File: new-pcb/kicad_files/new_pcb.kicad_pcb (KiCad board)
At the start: 2 copper layers, 98 x 81.6 mm, 39 parts, among them K0 KEYSW, K1 KEYSW, K10 KEYSW, K11 KEYSW, K12 KEYSW, K13 KEYSW, K2 KEYSW, K20 KEYSW, K21 KEYSW, K22 KEYSW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

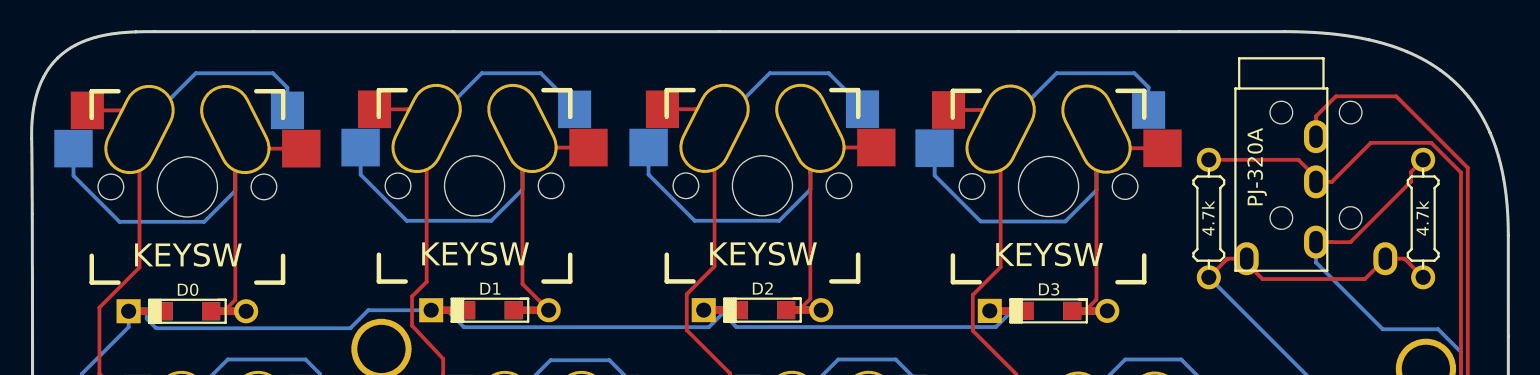
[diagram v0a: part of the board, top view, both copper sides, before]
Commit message: Add filled zones.
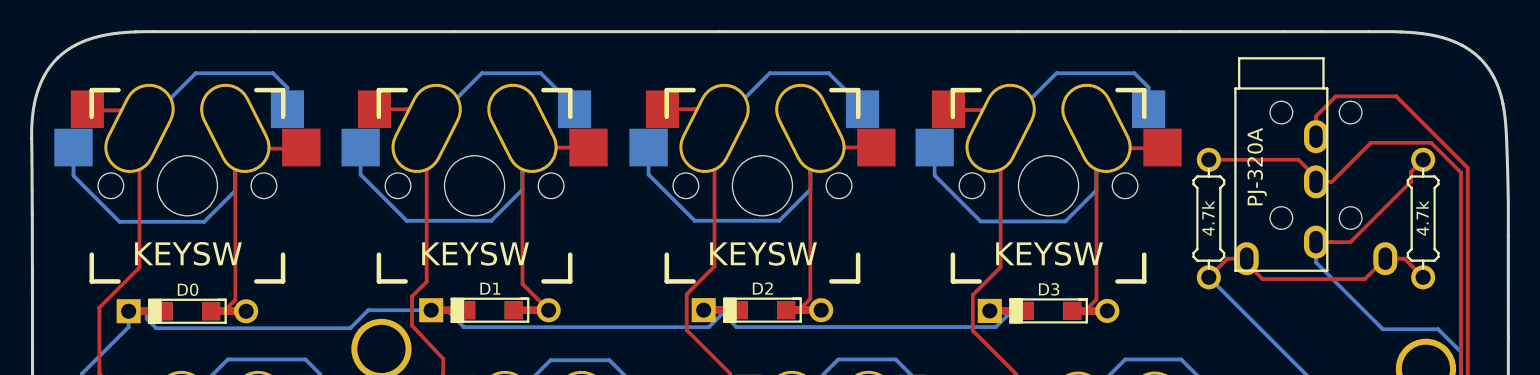
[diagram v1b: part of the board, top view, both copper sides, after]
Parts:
- moved K0 0.08 mm to (92.1, 60.9)
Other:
- outline, holes or cut-outs redrawn
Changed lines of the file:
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@@
-(kicad_pcb (version 20171130) (host pcbnew "(6.0.0-rc1-dev-1469-g932b9a334)")
+(kicad_pcb (version 20171130) (host pcbnew "(5.1.2-1)-1")
   (general
     (thickness 1.6)
-    (drawings 127)
+    (drawings 130)
     (tracks 420)
     (zones 0)
@@
   )
   (module new_pcb_footprints:Mx_hotswappable_oval (layer F.Cu)
-    (at 111.18 60.935)
+    (at 111.18 60.93)
     (descr "MX-style keyswitch with Kailh socket mount")
     (tags MX,cherry,gateron,kailh,pg1511,socket)
@@
   )
   (module new_pcb_footprints:Mx_hotswappable_oval (layer F.Cu)
-    (at 149.28 60.98)
+    (at 149.28 60.93)
     (descr "MX-style keyswitch with Kailh socket mount")
     (tags MX,cherry,gateron,kailh,pg1511,socket)
@@
   )
   (module new_pcb_footprints:Mx_hotswappable_oval (layer F.Cu)
-    (at 92.12 61.005)
+    (at 92.12 60.93)
     (descr "MX-style keyswitch with Kailh socket mount")
     (tags MX,cherry,gateron,kailh,pg1511,socket)
@@
       (xy -9.943822 1.795852)) (layer B.SilkS) (width 0.01))
   )
+  (gr_curve (pts (xy 179.68 57.76) (xy 179.642139 56.916852) (xy 179.574452 56.146128) (xy 179.437228 55.471054)) (layer Edge.Cuts) (width 0.2))
+  (gr_curve (pts (xy 179.437228 55.471054) (xy 179.300004 54.79598) (xy 179.093242 54.216556) (xy 178.832014 53.719231)) (layer Edge.Cuts) (width 0.2))
+  (gr_curve (pts (xy 178.832014 53.719231) (xy 178.570786 53.221906) (xy 178.255091 52.80668) (xy 177.9 52.46)) (layer Edge.Cuts) (width 0.2))
+  (gr_curve (pts (xy 177.9 52.46) (xy 177.54491 52.113321) (xy 177.150423 51.835189) (xy 176.731612 51.612052)) (layer Edge.Cuts) (width 0.2))
+  (gr_curve (pts (xy 176.731612 51.612052) (xy 176.312801 51.388916) (xy 175.869664 51.220774) (xy 175.417274 51.094077)) (layer Edge.Cuts) (width 0.2))
+  (gr_curve (pts (xy 175.417274 51.094077) (xy 174.964884 50.967379) (xy 174.50324 50.882126) (xy 174.047412 50.824764)) (layer Edge.Cuts) (width 0.2))
+  (gr_curve (pts (xy 174.047412 50.824764) (xy 173.591585 50.767402) (xy 173.141574 50.737933) (xy 172.712451 50.722803)) (layer Edge.Cuts) (width 0.2))
+  (gr_curve (pts (xy 167.42 50.7) (xy 166.87 50.7) (xy 165.71 50.7) (xy 164.916487 50.7)) (layer Edge.Cuts) (width 0.2))
   (gr_curve (pts (xy 161.095614 128.694384) (xy 160.159829 128.694384) (xy 159.401227 127.935779) (xy 159.401227 127)) (layer Eco1.User) (width 0.2))
   (gr_curve (pts (xy 159.401227 127) (xy 159.401227 126.064221) (xy 160.159829 125.305616) (xy 161.095614 125.305616)) (layer Eco1.User) (width 0.2))
@@
   (gr_curve (pts (xy 179.8 70.963392) (xy 179.8 73.928609) (xy 179.8 77.531869) (xy 179.8 81.539302)) (layer Edge.Cuts) (width 0.2))
   (gr_curve (pts (xy 179.795992 64.215737) (xy 179.794445 65.671001) (xy 179.796172 67.998175) (xy 179.800281 70.963392)) (layer Edge.Cuts) (width 0.2))
-  (gr_curve (pts (xy 179.482085 60.429541) (xy 179.688777 61.562322) (xy 179.797475 62.820181) (xy 179.795992 64.215737)) (layer Edge.Cuts) (width 0.2))
-  (gr_curve (pts (xy 178.580213 57.393816) (xy 178.970707 58.289058) (xy 179.275393 59.296761) (xy 179.482085 60.429541)) (layer Edge.Cuts) (width 0.2))
-  (gr_curve (pts (xy 177.163498 55.032848) (xy 177.713419 55.71579) (xy 178.18972 56.498573) (xy 178.580213 57.393816)) (layer Edge.Cuts) (width 0.2))
-  (gr_curve (pts (xy 175.305059 53.270926) (xy 175.990034 53.766805) (xy 176.613576 54.349906) (xy 177.163498 55.032848)) (layer Edge.Cuts) (width 0.2))
-  (gr_curve (pts (xy 173.078018 52.032338) (xy 173.873674 52.366391) (xy 174.620083 52.775048) (xy 175.305059 53.270926)) (layer Edge.Cuts) (width 0.2))
-  (gr_curve (pts (xy 170.555495 51.241371) (xy 171.437458 51.438836) (xy 172.282361 51.698285) (xy 173.078018 52.032338)) (layer Edge.Cuts) (width 0.2))
-  (gr_curve (pts (xy 167.810611 50.822314) (xy 168.754508 50.908427) (xy 169.673531 51.043907) (xy 170.555495 51.241371)) (layer Edge.Cuts) (width 0.2))
-  (gr_curve (pts (xy 164.916487 50.699453) (xy 165.897944 50.699453) (xy 166.866714 50.7362) (xy 167.810611 50.822314)) (layer Edge.Cuts) (width 0.2))
+  (gr_curve (pts (xy 179.68 57.76) (xy 179.83 61.69) (xy 179.797475 62.820181) (xy 179.795992 64.215737)) (layer Edge.Cuts) (width 0.2))
+  (gr_curve (pts (xy 170.53 50.7) (xy 171.437458 50.7) (xy 172.11 50.69) (xy 172.712451 50.722803)) (layer Edge.Cuts) (width 0.2))
+  (gr_curve (pts (xy 167.42 50.7) (xy 168.82 50.7) (xy 169.73 50.7) (xy 170.53 50.7)) (layer Edge.Cuts) (width 0.2))
   (gr_curve (pts (xy 157.98 50.7) (xy 161.501952 50.699453) (xy 163.935031 50.699453) (xy 164.916487 50.699453)) (layer Edge.Cuts) (width 0.2))
   (gr_curve (pts (xy 147.305545 50.699453) (xy 154.063878 50.699453) (xy 156.829614 50.699453) (xy 157.96 50.699453)) (layer Edge.Cuts) (width 0.2))

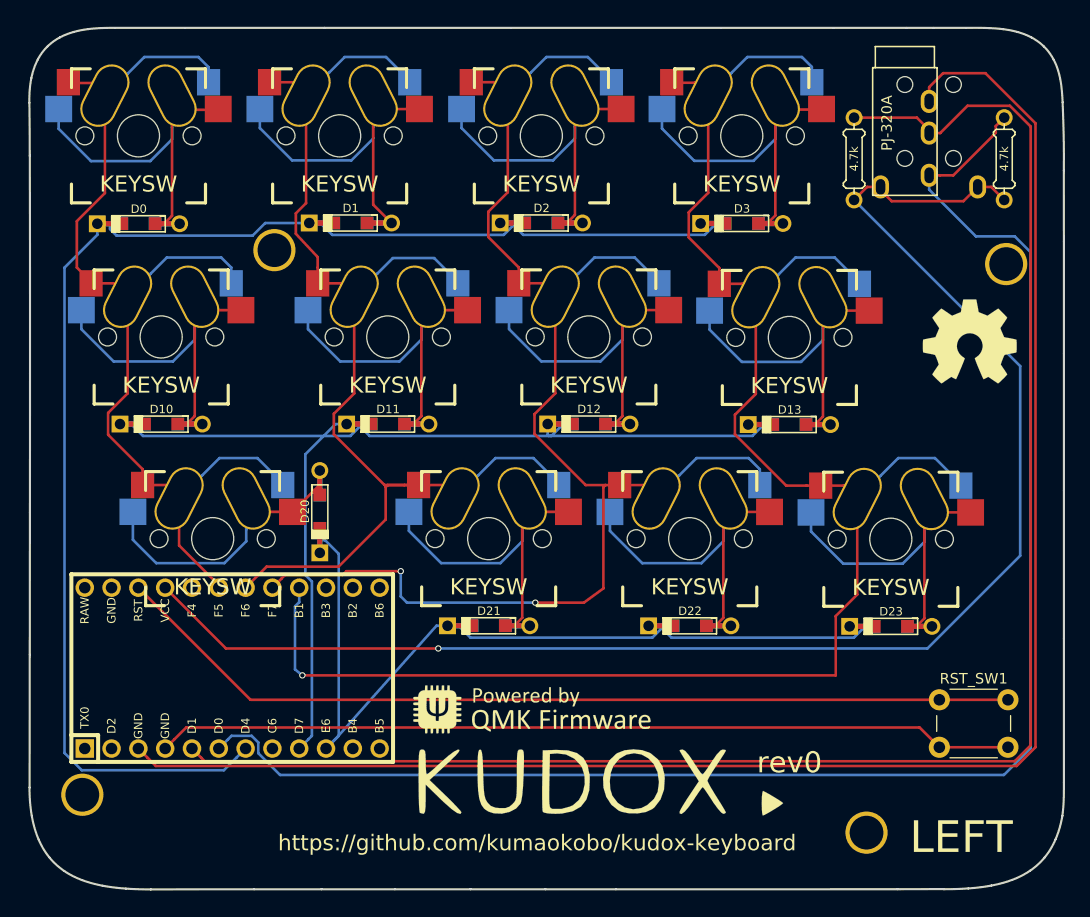
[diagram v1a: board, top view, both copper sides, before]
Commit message: Modified kudox-xs and new-pcb.
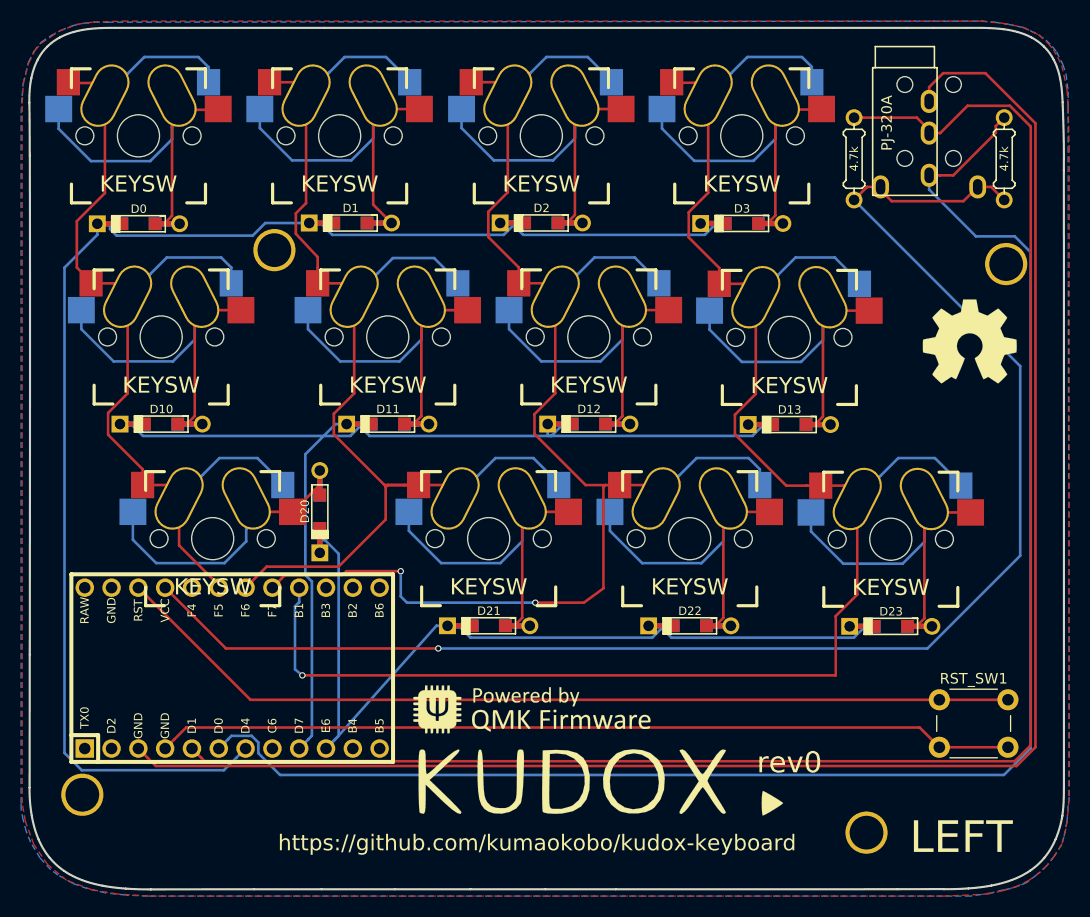
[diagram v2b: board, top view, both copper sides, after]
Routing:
- added copper zone on B.Cu, net (none)
- added copper zone on F.Cu, net (none)
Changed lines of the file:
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@@
-(kicad_pcb (version 20171130) (host pcbnew "(5.1.2-1)-1")
+(kicad_pcb (version 20171130) (host pcbnew "(6.0.0-rc1-dev-1469-g932b9a334)")
   (general
     (thickness 1.6)
@@
   (segment (start 102.73 114.36) (end 92.11 103.74) (width 0.25) (layer F.Cu) (net 30))
   (segment (start 168 114.36) (end 102.73 114.36) (width 0.25) (layer F.Cu) (net 30))
+  (zone (net 0) (net_name "") (layer F.Cu) (hatch edge 0.508)
+    (connect_pads (clearance 0.508))
+    (min_thickness 0.254)
+    (fill yes (arc_segments 16) (thermal_gap 0.508) (thermal_bridge_width 0.508))
+    (polygon
+      (pts
+        (xy 180.3 61.96) (xy 180.3 123.76) (xy 180.2 124.86) (xy 180 126.56) (xy 179.6 128.06)
+        (xy 178.9 129.16) (xy 178.2 130.06) (xy 177.6 130.66) (xy 176.5 131.46) (xy 175.3 132.06)
+        (xy 174 132.46) (xy 172.6 132.76) (xy 170.7 132.86) (xy 168.5 132.96) (xy 93.1 132.96)
+        (xy 90.1 132.76) (xy 87.7 132.36) (xy 85.3 131.46) (xy 83.5 129.96) (xy 82.2 128.06)
+        (xy 81.4 125.86) (xy 81.1 124.16) (xy 81.1 57.86) (xy 81.2 56.06) (xy 81.7 54.06)
+        (xy 82.3 52.86) (xy 82.9 52.16) (xy 83.8 51.56) (xy 84.5 51.06) (xy 86.3 50.36)
+        (xy 87.8 50.16) (xy 90.6 50.06) (xy 171.9 50.06) (xy 174 50.26) (xy 176 50.66)
+        (xy 177.4 51.36) (xy 178.3 52.16) (xy 178.8 52.76) (xy 179.2 53.46) (xy 179.6 54.26)
+        (xy 179.8 55.16) (xy 180.1 56.56) (xy 180.2 58.16)
+      )
+    )
+  )
+  (zone (net 0) (net_name "") (layer B.Cu) (hatch edge 0.508)
+    (connect_pads (clearance 0.508))
+    (min_thickness 0.254)
+    (fill yes (arc_segments 16) (thermal_gap 0.508) (thermal_bridge_width 0.508))
+    (polygon
+      (pts
+        (xy 180.2 61.96) (xy 180.3 123.56) (xy 180.2 124.36) (xy 180.1 125.86) (xy 179.8 127.36)
+        (xy 179.6 128.06) (xy 178.9 129.16) (xy 178.2 130.06) (xy 177.2 130.96) (xy 176.3 131.66)
+        (xy 175.6 131.96) (xy 174.7 132.26) (xy 174.1 132.36) (xy 172.9 132.66) (xy 171 132.96)
+        (xy 93 132.96) (xy 90.9 132.86) (xy 89 132.66) (xy 87.3 132.26) (xy 85.9 131.76)
+        (xy 84.5 130.96) (xy 83.8 130.46) (xy 82.8 129.36) (xy 81.9 127.86) (xy 81.5 126.86)
+        (xy 81.2 125.76) (xy 81 124.76) (xy 81 124.16) (xy 81 58.76) (xy 81.1 57.16)
+        (xy 81.2 55.96) (xy 81.7 53.96) (xy 82.2 52.96) (xy 82.9 52.06) (xy 83.8 51.46)
+        (xy 84.7 50.96) (xy 86 50.46) (xy 86.9 50.26) (xy 87.9 50.16) (xy 89.2 50.16)
+        (xy 172 50.06) (xy 173.2 50.16) (xy 174.5 50.36) (xy 175.9 50.66) (xy 176.6 50.96)
+        (xy 177.4 51.36) (xy 178.1 51.86) (xy 178.7 52.46) (xy 179.1 52.96) (xy 179.7 54.16)
+        (xy 180 55.06) (xy 180.2 56.76) (xy 180.2 58.26)
+      )
+    )
+  )
 )
